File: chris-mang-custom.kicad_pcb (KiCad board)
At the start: 2 copper layers, 110 x 63.3 mm, 151 parts, among them J1 Barrel_Jack_Switch, J2 AudioJack_TRS, J3 AudioJack_TRS, J4 Conn_01x06, J5 Conn_01x06, Q1 Q_PMOS_GSD, Q2 2N7002, Q3 2N7002, Q4 2N7002, Q5 LS844, Q6 BC858C, Q7 LS844, Q8 BC858C, Q9 BC848C, SW1 SW_SPDT, SW2 SW_DPDT_x2, SW3 SW_DIP_SPDT_2pos, U1 DG412xY, U2 OPA2134, U3 TLV9352, U4 TLV9352

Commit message: first route of PCB
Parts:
- removed C34, C36: 8.2n, bca-footprints:C_Film_L7.2mm_W2.5mm_P5.00mm
- removed C35: 47p, Capacitor_SMD:C_0603_1608Metric_Pad1.08x0.95mm_HandSolder
- removed C37: 18n, bca-footprints:C_Film_L7.2mm_W2.5mm_P5.00mm
- removed C38: 39n, bca-footprints:C_Film_L7.2mm_W2.5mm_P5.00mm
- removed C39: 3.9n, bca-footprints:C_Film_L7.2mm_W2.5mm_P5.00mm
- removed C40: 5.6n, bca-footprints:C_Film_L7.2mm_W2.5mm_P5.00mm
- removed C41: 10u, Capacitor_SMD:C_0805_2012Metric_Pad1.18x1.45mm_HandSolder
- removed C42, C43: 100u, bca-footprints:CP_Radial_D6.3mm_P2.50mm
- removed C44, C45: 100n, Capacitor_SMD:C_0603_1608Metric_Pad1.08x0.95mm_HandSolder
- removed D12: 1N4148, Diode_SMD:D_SOD-323_HandSoldering
- removed Q7: LS844, Package_TO_SOT_SMD:SOT-23-6_Handsoldering
- removed Q8: BC858C, Package_TO_SOT_SMD:SOT-23_Handsoldering
- removed Q9: BC848C, Package_TO_SOT_SMD:SOT-23_Handsoldering
- removed R44: 15k, bca-footprints:R_L3.6mm_D1.6mm_P5.00mm_Horizontal
- removed R45, R58, R59: 10k, bca-footprints:R_L3.6mm_D1.6mm_P5.00mm_Horizontal
- removed R46: 22k, bca-footprints:R_L3.6mm_D1.6mm_P5.00mm_Horizontal
- removed R47: 1.5k, bca-footprints:R_L3.6mm_D1.6mm_P5.00mm_Horizontal
- removed R48, R55: 470k, bca-footprints:R_L3.6mm_D1.6mm_P5.00mm_Horizontal
- removed R49, R51, R53: 1M, Resistor_SMD:R_0805_2012Metric_Pad1.20x1.40mm_HandSolder
- removed R50, R56: 1k, bca-footprints:R_L3.6mm_D1.6mm_P5.00mm_Horizontal
- removed R52: 33k, Resistor_SMD:R_0805_2012Metric_Pad1.20x1.40mm_HandSolder
- removed R54: 6.8k, bca-footprints:R_L3.6mm_D1.6mm_P5.00mm_Horizontal
- removed R57: 100k, bca-footprints:R_L3.6mm_D1.6mm_P5.00mm_Horizontal
- removed R60, R61: 10k, Resistor_SMD:R_0805_2012Metric_Pad1.20x1.40mm_HandSolder
- removed SW3: SW_DIP_SPDT_2pos, bca-footprints:DIP-8_W7.62mm_Socket
- added RV9: 100kA, bca-footprints:R_POT, F.Cu at (45.0, -2.00)
- C14: footprint Capacitor_SMD:C_0603_1608Metric_Pad1.08x0.95mm_HandSolder -> Capacitor_SMD:C_0805_2012Metric_Pad1.18x1.45mm_HandSolder
- C16: value 0.15u -> 10n; footprint bca-footprints:C_Film_L7.2mm_W3.5mm_P5.00mm -> bca-footprints:C_Film_L7.2mm_W2.5mm_P5.00mm
- C17: value 47p -> 10n; footprint Capacitor_SMD:C_0603_1608Metric_Pad1.08x0.95mm_HandSolder -> bca-footprints:C_Film_L7.2mm_W2.5mm_P5.00mm
- C18: value 47p -> 100p; footprint Capacitor_SMD:C_0603_1608Metric_Pad1.08x0.95mm_HandSolder -> bca-footprints:C_Ceramic_L4.0mm_W2.5mm_P2.50mm
- C19: value 220p -> 0.1u; footprint bca-footprints:C_Ceramic_L4.0mm_W2.5mm_P2.50mm -> bca-footprints:C_Film_L7.2mm_W2.5mm_P5.00mm
- C20: value 0.1u -> 10n
- C21: value 47n -> 10n
- C22: value 3.9n -> 1u; footprint bca-footprints:C_Film_L7.2mm_W2.5mm_P5.00mm -> bca-footprints:C_Film_L7.2mm_W3.5mm_P5.00mm
- C23: footprint bca-footprints:C_Film_L7.2mm_W3.5mm_P5.00mm -> bca-footprints:CP_Radial_D4.0mm_P1.50mm
- C24, C25: value 100p -> 0.1u; footprint Capacitor_SMD:C_0603_1608Metric_Pad1.08x0.95mm_HandSolder -> bca-footprints:C_Film_L7.2mm_W2.5mm_P5.00mm
- C26: value 5.6n -> 22p; footprint bca-footprints:C_Film_L7.2mm_W2.5mm_P5.00mm -> bca-footprints:C_Ceramic_L4.0mm_W2.5mm_P2.50mm
- C27: value 5.6n -> 10u; footprint bca-footprints:C_Film_L7.2mm_W2.5mm_P5.00mm -> bca-footprints:CP_Radial_D4.0mm_P1.50mm
- C28: value 18n -> 10n
- C29: value 68n -> 10u; footprint bca-footprints:C_Film_L7.2mm_W2.5mm_P5.00mm -> bca-footprints:CP_Radial_D4.0mm_P1.50mm
- C30: value 33n -> 100u; footprint bca-footprints:C_Film_L7.2mm_W2.5mm_P5.00mm -> bca-footprints:CP_Radial_D6.3mm_P2.50mm
- C31: value 22p -> 100u; footprint Capacitor_SMD:C_0603_1608Metric_Pad1.08x0.95mm_HandSolder -> bca-footprints:CP_Radial_D6.3mm_P2.50mm
- C32: value 10u -> 100n
- C33: value 5.6n -> 100n; footprint bca-footprints:C_Film_L7.2mm_W2.5mm_P5.00mm -> Capacitor_SMD:C_0805_2012Metric_Pad1.18x1.45mm_HandSolder
- C6, C9: footprint Capacitor_SMD:C_0603_1608Metric_Pad1.08x0.95mm_HandSolder -> bca-footprints:C_Ceramic_L4.0mm_W2.5mm_P2.50mm
- D10: value 4v7 Zener -> 1N4148; footprint Diode_SMD:D_SOD-323_HandSoldering -> bca-footprints:Diode_DO-35_P5.00mm
- D11: value 1N4148 -> 1N5711; footprint Diode_SMD:D_SOD-323_HandSoldering -> bca-footprints:Diode_DO-35_P5.00mm
- D2, D3, D4, D5, D7, D8: footprint Diode_SMD:D_SOD-323_HandSoldering -> bca-footprints:Diode_DO-35_P5.00mm
- D6: value 1N5711 -> 1N4148; footprint Diode_SMD:D_SOD-323_HandSoldering -> bca-footprints:Diode_DO-35_P5.00mm
- D9: value 3v3 Zener -> 1N4148; footprint Diode_SMD:D_SOD-323_HandSoldering -> bca-footprints:Diode_DO-35_P5.00mm
- Q5: value LS844 -> BC848C; footprint Package_TO_SOT_SMD:SOT-23-6_Handsoldering -> Package_TO_SOT_SMD:SOT-23_Handsoldering
- Q6: value BC858C -> BC848C
- R19: value 10k -> 1M
- R20: value 1M -> 10k; footprint Resistor_SMD:R_0805_2012Metric_Pad1.20x1.40mm_HandSolder -> bca-footprints:R_L3.6mm_D1.6mm_P5.00mm_Horizontal
- R21: value 2.2k -> 27k; footprint Resistor_SMD:R_0603_1608Metric_Pad0.98x0.95mm_HandSolder -> bca-footprints:R_L3.6mm_D1.6mm_P5.00mm_Horizontal
- R22: value 4.7k -> 33k; footprint Resistor_SMD:R_0603_1608Metric_Pad0.98x0.95mm_HandSolder -> bca-footprints:R_L3.6mm_D1.6mm_P5.00mm_Horizontal
- R23: value 1.5k -> 1M
- R24: value 15k -> 10k
- R25, R31, R35: value 2.2k -> 100k; footprint Resistor_SMD:R_0603_1608Metric_Pad0.98x0.95mm_HandSolder -> bca-footprints:R_L3.6mm_D1.6mm_P5.00mm_Horizontal
- R26: value 56k -> 10k
- R27: value 330k -> 6.8k
- R28: value 1M -> 220k
- R29: value 15k -> 1k
- R30: value 470k -> 6.8k
- R32: value 4.7k -> 1M; footprint Resistor_SMD:R_0603_1608Metric_Pad0.98x0.95mm_HandSolder -> bca-footprints:R_L3.6mm_D1.6mm_P5.00mm_Horizontal
- R33: value 3.9k -> 10k
- R34: value 33k -> 100k
- R36: value 1k -> 100k
- R37: value 6.8k -> 10k
- R38: value 5.6k -> 1k
- R39: value 3.9k -> 1M
- R40: value 470k -> 10k
- R41: value 180k -> 22k
- R42: footprint bca-footprints:R_L3.6mm_D1.6mm_P5.00mm_Horizontal -> Resistor_SMD:R_0805_2012Metric_Pad1.20x1.40mm_HandSolder
- R43: value 22k -> 10k; footprint bca-footprints:R_L3.6mm_D1.6mm_P5.00mm_Horizontal -> Resistor_SMD:R_0805_2012Metric_Pad1.20x1.40mm_HandSolder
- RV5: value 250kA -> 100kB; footprint bca-footprints:R_POT_DUAL -> bca-footprints:R_POT
- RV6: value 100kA -> 25kB
- RV7: value 100k-CD -> 100kA; footprint bca-footprints:R_POT -> bca-footprints:R_POT_9mm
- RV8: value 100k-CD -> 100kA
- SW2: value SW_DPDT_x2 -> SW_DIP_SPDT_2pos; footprint bca-footprints:SW_Toggle_DPDT_SolderLug -> bca-footprints:DIP-8_W7.62mm_Socket; moved to F.Cu
- U3: value TLV9352 -> NJM4580
- moved Q5 60.6 mm to (50.6, -9.60)
- moved R43 56.3 mm to (17.2, -38.6), turned to -90 degrees
- moved R42 55.5 mm to (15.3, -38.6), turned to 90 degrees
- moved R34 53.4 mm to (50.6, -4.19), turned to 0 degrees
- moved R33 53.4 mm to (50.6, -6.47)
- moved Q6 51.9 mm to (50.6, 5.99)
- moved R39 51.7 mm to (50.6, 11.4), turned to 180 degrees
- moved R36 49.0 mm to (50.6, 0.36)
- moved C16 47.1 mm to (21.1, -28.5), turned to 180 degrees
- moved C15 46.7 mm to (21.1, -31.9), turned to 180 degrees
- moved R35 44.2 mm to (50.6, -1.92), turned to 0 degrees
- moved C28 43.7 mm to (40.9, 11.0), turned to 0 degrees
- moved R31 43.3 mm to (8.50, 10.3), turned to 180 degrees
- moved C27 42.0 mm to (38.7, 7.00), turned to 90 degrees
- moved RV6 41.0 mm to (15.0, -2.00)
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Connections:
- C15 pad 1: Net-(C15-Pad1) -> Earth
- C15 pad 2: Net-(Q5B-G1) -> Net-(C15-Pad2)
- C16 pad 1: Net-(C16-Pad1) -> Net-(C15-Pad2)
- C16 pad 2: Earth -> Net-(C16-Pad2)
- C17 pad 1: Net-(Q5A-G1) -> Net-(C17-Pad1)
- C17 pad 2: Net-(Q6-C) -> Net-(U3B-+)
- C18 pad 1: Net-(Q5B-D2) -> /bluesbreaker/sw2
- C18 pad 2: Net-(Q6-C) -> Net-(C18-Pad2)
- C19 pad 1: Net-(Q6-C) -> Net-(C19-Pad1)
- C20 pad 1: Net-(C20-Pad1) -> /bluesbreaker/4.5V
- C20 pad 2: Net-(D5-K) -> Net-(C20-Pad2)
- C21 pad 1: Net-(C20-Pad1) -> /bluesbreaker/4.5V
- C22 pad 1: Net-(D5-K) -> Net-(C22-Pad1)
- C22 pad 2: Net-(Q7B-G1) -> Net-(Q5-B)
- C23 pad 1: Net-(C23-Pad1) -> Net-(C22-Pad1)
- C23 pad 2: Earth -> Net-(Q5-B)
- C24 pad 1: Net-(D9-A) -> Net-(Q5-E)
- C24 pad 2: /blues-driver/sw_8 -> Net-(C24-Pad2)
- C25 pad 1: Net-(Q7B-D2) -> Net-(C25-Pad1)
- C25 pad 2: /blues-driver/sw_8 -> Net-(C25-Pad2)
- C26 pad 1: /blues-driver/sw_8 -> Net-(U4B--)
- C27 pad 1: Earth -> Net-(C26-Pad2)
- C28 pad 1: Earth -> /bluesbreaker-send
- C28 pad 2: Net-(C28-Pad2) -> Net-(Q6-B)
- C29 pad 1: /blues-driver/sw_6 -> Net-(Q6-E)
- C30 pad 1: /blues-driver/sw_3 -> /bluesbreaker/9V
- C30 pad 2: Net-(C29-Pad2) -> Earth
- C31 pad 1: Net-(U3B--) -> /bluesbreaker/4.5V
- C31 pad 2: Net-(C31-Pad2) -> Earth
- C32 pad 1: Net-(C31-Pad2) -> /bluesbreaker/9V
- C32 pad 2: /blues-driver/vol_out -> Earth
- C33 pad 1: Net-(U3A--) -> /bluesbreaker/9V
- C33 pad 2: Net-(C33-Pad2) -> Earth
- D10 pad 2: /blues-driver/sw_1 -> Net-(D10-A)
- D11 pad 1: Net-(D11-K) -> /bluesbreaker/sw3
- D11 pad 2: Net-(D11-A) -> Net-(D10-K)
- D6 pad 2: Earth -> Net-(D6-A)
- D7 pad 1: Net-(D7-K) -> /bluesbreaker/sw4
- D8 pad 1: Net-(D7-K) -> Net-(D6-A)
- D8 pad 2: Earth -> /bluesbreaker/sw4
- D9 pad 1: Net-(D10-K) -> Net-(D10-A)
- D9 pad 2: Net-(D9-A) -> /bluesbreaker/sw3
- FB3 pad 2: /blues-driver/9V -> /bluesbreaker/9V
- J5 pad 3: /bluesdriver-send -> /bluesbreaker-send
- J5 pad 4: /bluesdriver-return -> /bluesbreaker-return
- Q5 pad 1: Net-(Q5A-G1) -> Net-(Q5-B)
- Q5 pad 2: /blues-driver/9V -> Net-(Q5-E)
- Q5 pad 3: Net-(Q5A-S1) -> /bluesbreaker/9V
- Q6 pad 1: Net-(Q5B-D2) -> Net-(Q6-B)
- Q6 pad 2: /blues-driver/9V -> Net-(Q6-E)
- Q6 pad 3: Net-(Q6-C) -> /bluesbreaker/9V
- R19 pad 1: /bluesdriver-send -> Earth
- R19 pad 2: Net-(C15-Pad1) -> /bluesbreaker-send
- R20 pad 1: /blues-driver/4.5V -> /bluesbreaker-send
- R20 pad 2: Net-(Q5B-G1) -> Net-(C17-Pad1)
- R21 pad 1: Net-(Q5B-D2) -> Net-(C15-Pad2)
- R21 pad 2: /blues-driver/9V -> /bluesbreaker/sw2
- R22 pad 1: Earth -> Net-(C16-Pad2)
- R22 pad 2: Net-(Q5A-S1) -> /bluesbreaker/sw2
- R23 pad 1: Net-(C16-Pad1) -> /bluesbreaker/4.5V
- R23 pad 2: Net-(Q5A-G1) -> Net-(U3B-+)
- R24 pad 1: Net-(Q5A-G1) -> /bluesbreaker/sw7
- R24 pad 2: Net-(RV5A-4) -> Net-(R24-Pad2)
- R25 pad 1: Earth -> /bluesbreaker/sw2
- R25 pad 2: Net-(Q6-C) -> Net-(R24-Pad2)
- R26 pad 1: Net-(C20-Pad1) -> Net-(C19-Pad2)
- R26 pad 2: Net-(Q6-C) -> Net-(U3A--)
- R27 pad 1: Net-(D5-K) -> Net-(U3A--)
- R27 pad 2: Net-(C19-Pad2) -> Net-(D5-A)
- R28 pad 1: Net-(C21-Pad2) -> Net-(U3A--)
- R28 pad 2: Net-(D5-K) -> /bluesbreaker/sw5
- R29 pad 1: Earth -> /bluesbreaker/sw5
- R29 pad 2: Net-(C21-Pad2) -> Net-(D10-A)
- R30 pad 1: /blues-driver/4.5V -> Net-(R30-Pad1)
- R30 pad 2: Net-(Q7B-G1) -> Net-(R30-Pad2)
- R31 pad 1: Net-(Q7B-D2) -> Net-(C21-Pad2)
- R31 pad 2: /blues-driver/9V -> Net-(R30-Pad2)
- R32 pad 1: Earth -> /bluesbreaker/4.5V
- R32 pad 2: Net-(Q7A-S1) -> Net-(Q5-B)
- R33 pad 1: Net-(C23-Pad1) -> Earth
- R33 pad 2: Net-(D9-A) -> Net-(Q5-E)
- R34 pad 1: Net-(D9-A) -> Net-(C24-Pad2)
- R34 pad 2: Net-(R34-Pad2) -> Net-(U4B--)
- R35 pad 1: Earth -> Net-(C25-Pad2)
- R35 pad 2: /blues-driver/sw_8 -> Net-(U4B--)
- R36 pad 1: Net-(C26-Pad2) -> Net-(U4B--)
- R36 pad 2: Net-(C27-Pad2) -> Net-(C26-Pad2)
- R37 pad 1: /blues-driver/sw_8 -> Earth
- R38 pad 2: /blues-driver/sw_3 -> /bluesbreaker-return
- R39 pad 1: Net-(C28-Pad2) -> /bluesbreaker/4.5V
- R39 pad 2: /blues-driver/sw_3 -> Net-(Q6-B)
- R40 pad 1: Net-(R40-Pad1) -> Earth
- R40 pad 2: Net-(U3B--) -> Net-(Q6-E)
- R41 pad 1: Net-(U3B--) -> Net-(C29-Pad2)
- R41 pad 2: Net-(C31-Pad2) -> Net-(U4A--)
- R42 pad 1: /blues-driver/vol_out -> /bluesbreaker/4.5V
- R42 pad 2: Net-(R42-Pad2) -> /bluesbreaker/9V
- R43 pad 1: /blues-driver/vol_out -> Earth
- R43 pad 2: Net-(C34-Pad2) -> /bluesbreaker/4.5V
- RV5 pad 1: Net-(RV5A-4) -> Net-(R24-Pad2)
- RV5 pad 2: Net-(Q6-C) -> Net-(C18-Pad2)
- RV5 pad 3: Net-(Q6-C) -> Net-(C19-Pad1)
- RV6 pad 1: /blues-driver/4.5V -> Net-(C20-Pad2)
- RV6 pad 2: Net-(R40-Pad1) -> Net-(R30-Pad1)
- RV6 pad 3: Net-(C29-Pad2) -> Net-(D10-A)
- RV7 pad 1: Net-(R45-Pad1) -> Net-(C21-Pad2)
- RV7 pad 2: Net-(C33-Pad2) -> Net-(R30-Pad2)
- RV7 pad 3: Net-(R42-Pad2) -> Net-(R30-Pad2)
- RV8 pad 1: Net-(C34-Pad1) -> /bluesbreaker/4.5V
- RV8 pad 2: Net-(R44-Pad1) -> Net-(C22-Pad1)
- RV8 pad 3: Net-(C34-Pad2) -> Net-(R30-Pad2)
- SW2 pad 1: Net-(SW2A-A) -> unconnected-(SW2A-C-Pad1)
- SW2 pad 2: Net-(D11-A) -> /bluesbreaker/sw2
- SW2 pad 3: Net-(SW2A-C) -> /bluesbreaker/sw3
- SW2 pad 4: Net-(SW2B-A) -> /bluesbreaker/sw4
- SW2 pad 5: Net-(D11-K) -> /bluesbreaker/sw5
- SW2 pad 6: unconnected-(SW2B-C-Pad6) -> /bluesbreaker/4.5V
- U3 pad 1: Net-(C35-Pad2) -> /bluesbreaker/sw5
- U3 pad 3: /blues-driver/4.5V -> /bluesbreaker/4.5V
- U3 pad 5: /blues-driver/4.5V -> Net-(U3B-+)
- U3 pad 6: Net-(U3B--) -> /bluesbreaker/sw2
- U3 pad 7: Net-(C31-Pad2) -> Net-(C18-Pad2)
- U3 pad 8: /blues-driver/9V -> /bluesbreaker/9V
- U4 pad 1: Net-(C39-Pad2) -> Net-(C25-Pad1)
- U4 pad 2: Net-(D11-K) -> Net-(U4A--)
- U4 pad 3: Net-(D11-A) -> /bluesbreaker/4.5V
- U4 pad 5: Net-(U4B-+) -> /bluesbreaker/4.5V
- U4 pad 7: Net-(U4B--) -> Net-(C26-Pad2)
- U4 pad 8: /blues-driver/9V -> /bluesbreaker/9V

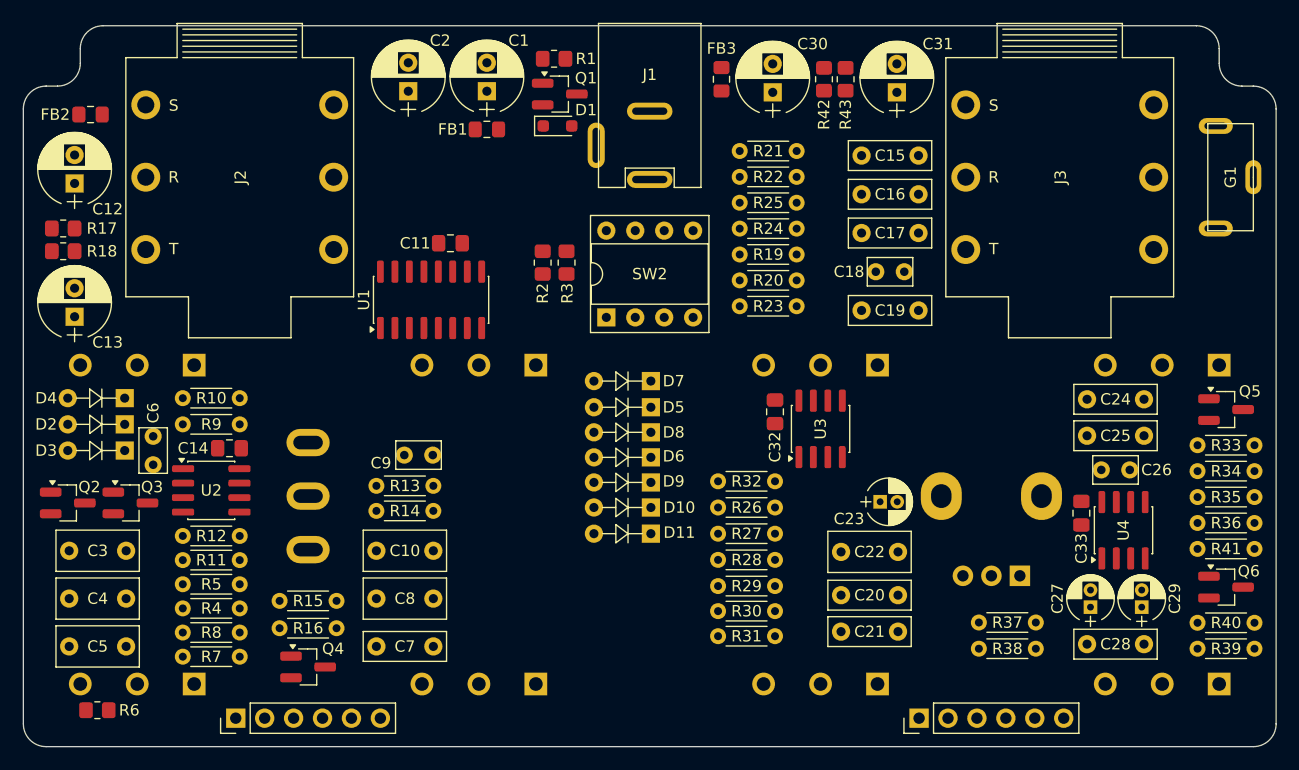
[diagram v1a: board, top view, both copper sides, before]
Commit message: finalized schematic
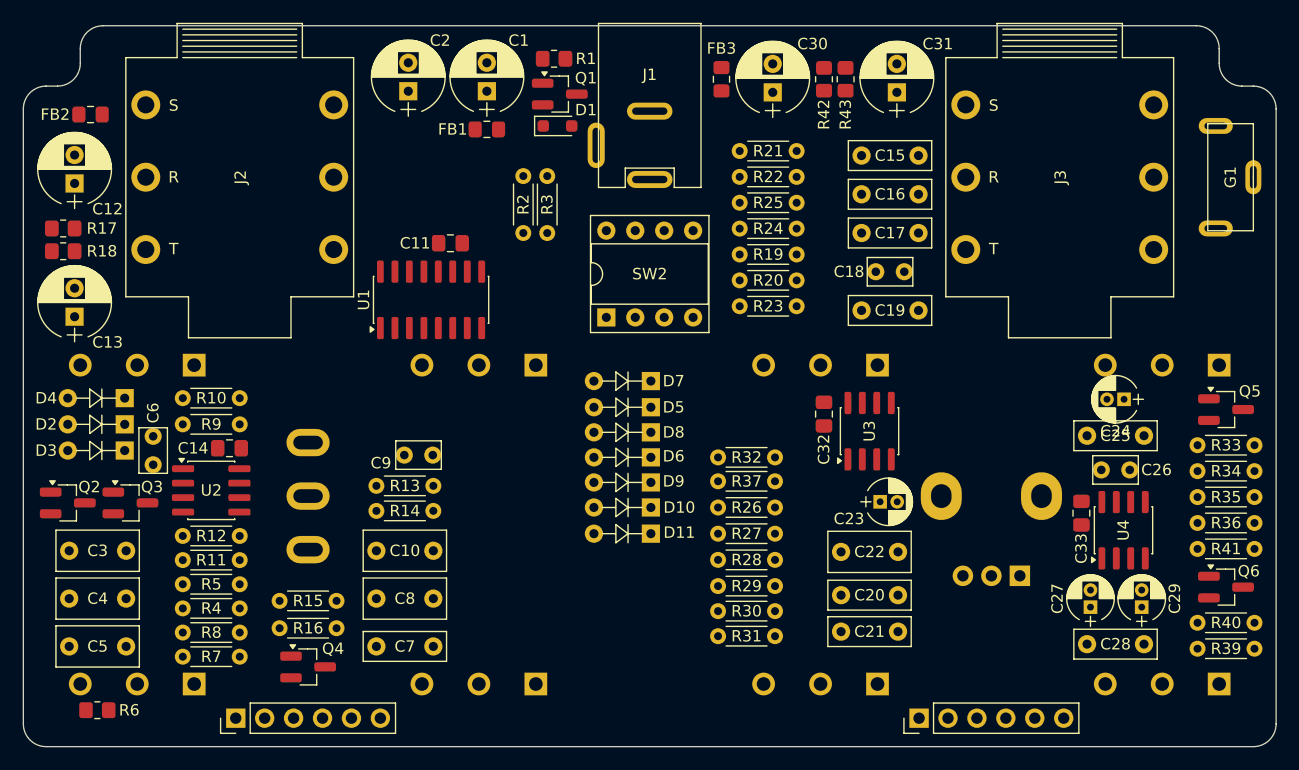
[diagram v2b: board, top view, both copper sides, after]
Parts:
- removed R38: 1k, bca-footprints:R_L3.6mm_D1.6mm_P5.00mm_Horizontal
- C24: value 0.1u -> 10u; footprint bca-footprints:C_Film_L7.2mm_W2.5mm_P5.00mm -> bca-footprints:CP_Radial_D4.0mm_P1.50mm
- C25: value 0.1u -> 47n
- C26: value 22p -> 47p
- R2, R3: footprint Resistor_SMD:R_0805_2012Metric_Pad1.20x1.40mm_HandSolder -> bca-footprints:R_L3.6mm_D1.6mm_P5.00mm_Horizontal
- R36: value 100k -> 180k
- R37: value 10k -> 100k
- R41: value 22k -> 10k
- moved R37 26.0 mm to (8.50, -3.30), turned to 0 degrees
- moved R3 5.38 mm to (-9.00, -27.6)
- moved R2 5.38 mm to (-11.1, -27.6)
- moved C32 4.30 mm to (15.3, -9.20)
- moved U3 4.30 mm to (19.3, -7.70)
- moved R32 2.10 mm to (8.50, -5.40)
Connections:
- R30 pad 2: Net-(R30-Pad2) -> Net-(C22-Pad1)
- R31 pad 2: Net-(R30-Pad2) -> Net-(C22-Pad1)
- R37 pad 1: Earth -> /bluesbreaker/4.5V
- R37 pad 2: Net-(C27-Pad2) -> Net-(C22-Pad1)
- RV7 pad 2: Net-(R30-Pad2) -> Net-(C22-Pad1)
- RV7 pad 3: Net-(R30-Pad2) -> Net-(C22-Pad1)
- RV8 pad 1: /bluesbreaker/4.5V -> Earth
- RV8 pad 2: Net-(C22-Pad1) -> /bluesbreaker-return
- RV8 pad 3: Net-(R30-Pad2) -> Net-(C27-Pad2)

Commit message: first draft PCB
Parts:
- added C34: 100p, bca-footprints:C_Ceramic_L4.0mm_W2.5mm_P2.50mm, F.Cu at (50.0, -1.30)
- R24: value 10k -> 33k
- R25: value 100k -> 150k
- moved C27 27.7 mm to (49.7, -18.4), turned to 0 degrees
- moved R33 24.6 mm to (26.4, -10.6), turned to 0 degrees
- moved Q5 23.1 mm to (27.7, -6.90)
- moved R31 21.6 mm to (30.0, 8.20)
- moved R39 20.6 mm to (30.0, 11.2), turned to 0 degrees
- moved R32 19.5 mm to (26.5, -12.8)
- moved Q4 18.6 mm to (-11.7, 9.80)
- moved R15 18.6 mm to (-11.7, 4.00), turned to 180 degrees
- moved R16 18.6 mm to (-11.7, 6.40), turned to 180 degrees
- moved R10 9.39 mm to (-30.0, -14.6)
- moved R4 9.25 mm to (-30.0, 11.5), turned to 180 degrees
- moved R9 8.95 mm to (-30.0, -11.1)
- moved R26 8.90 mm to (8.50, -9.90)
- moved R5 8.85 mm to (-30.0, 8.20)
- moved R27 8.24 mm to (8.50, -6.94)
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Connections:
- C18 pad 1: /bluesbreaker/sw2 -> /bluesbreaker/sw7
- R21 pad 2: /bluesbreaker/sw2 -> /bluesbreaker/sw7
- R22 pad 2: /bluesbreaker/sw2 -> /bluesbreaker/sw7
- R24 pad 1: /bluesbreaker/sw7 -> /bluesbreaker/sw2
- R25 pad 1: /bluesbreaker/sw2 -> /bluesbreaker/sw7
- U1 pad 1: /Zendrive/Q1D -> /Zendrive/Q1G
- U1 pad 10: Net-(D2-A) -> Net-(C4-Pad1)
- U1 pad 11: Net-(D4-A) -> Earth
- U1 pad 14: (no net) -> Net-(D4-A)
- U1 pad 15: (no net) -> Net-(D2-A)
- U1 pad 16: (no net) -> /Zendrive/Q1D
- U1 pad 2: Net-(C4-Pad1) -> Net-(R9-Pad2)
- U1 pad 3: Earth -> Net-(D4-A)
- U1 pad 6: Net-(R9-Pad2) -> (no net)
- U1 pad 7: Net-(D4-A) -> (no net)
- U1 pad 8: /Zendrive/Q1G -> (no net)
- U3 pad 6: /bluesbreaker/sw2 -> /bluesbreaker/sw7
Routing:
- net /bluesbreaker/4.5V: track 0.00 -> 170.2 mm, vias 0 -> 3
- net /bluesbreaker/9V: track 0.00 -> 122.8 mm, vias 0 -> 4
- net /Zendrive/9V: track 0.00 -> 110.1 mm, vias 0 -> 2
- net /bluesbreaker-send: track 0.00 -> 104.3 mm
- net +9V: track 0.00 -> 101.2 mm
- net /V+1: track 0.00 -> 90.3 mm
- net Net-(C4-Pad1): track 0.00 -> 89.9 mm, vias 0 -> 1
- net /output_jack: track 0.00 -> 86.3 mm
- net Net-(D4-A): track 0.00 -> 83.9 mm, vias 0 -> 2
- net /input_jack: track 0.00 -> 69.9 mm
- net /Zendrive/Q1G: track 0.00 -> 67.6 mm, vias 0 -> 1
- net /bluesbreaker-return: track 0.00 -> 64.2 mm
- net /bluesbreaker/sw7: track 0.00 -> 63.1 mm
- net Net-(D3-A): track 0.00 -> 62.1 mm
- net /V+0: track 0.00 -> 61.6 mm
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- added copper zone on In1.Cu, net Earth
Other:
- copper layers 2 -> 4

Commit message: generated gerbers
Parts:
- C22: footprint bca-footprints:C_Film_L7.2mm_W3.5mm_P5.00mm -> bca-footprints:C_Film_L7.2mm_W5.00mm_P5.00mm
- R24: value 33k -> 39k
- moved C20 1.30 mm to (18.6, 8.10)
- moved C28 1.00 mm to (40.1, 11.1)
- moved C29 0.81 mm to (40.1, 6.60)
- moved C22 0.80 mm to (18.6, 3.80)
- moved C21 0.50 mm to (18.6, 11.1)
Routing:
- net Net-(C22-Pad1): track 34.9 -> 37.4 mm
- net Net-(Q6-B): track 33.8 -> 32.2 mm
- net /bluesbreaker/4.5V: track 170.2 -> 168.6 mm
- net Net-(C20-Pad2): track 8.90 -> 7.60 mm
- net Net-(C4-Pad1): track 89.9 -> 88.6 mm
- net Net-(Q5-B): track 20.6 -> 21.4 mm
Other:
- board text added: "Bennett Custom Audio Custom Dual OD v1.0.0; Mar 2026"
- board text added: "Designed & Assembled in St. John's, NL"
- board text added: "HI GAIN ->"
- board text added: "OD -> DIST"

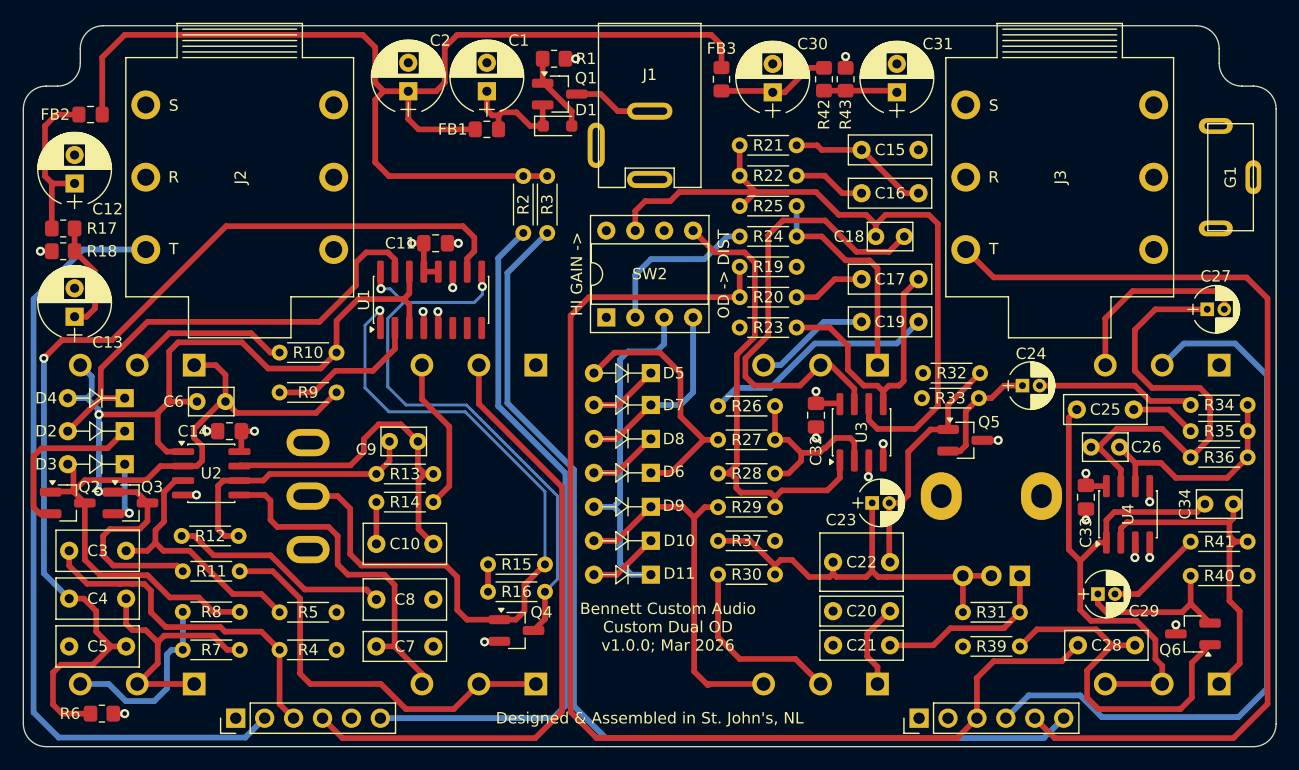
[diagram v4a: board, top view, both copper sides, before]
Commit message: re-generated gerbers, finalized BOM
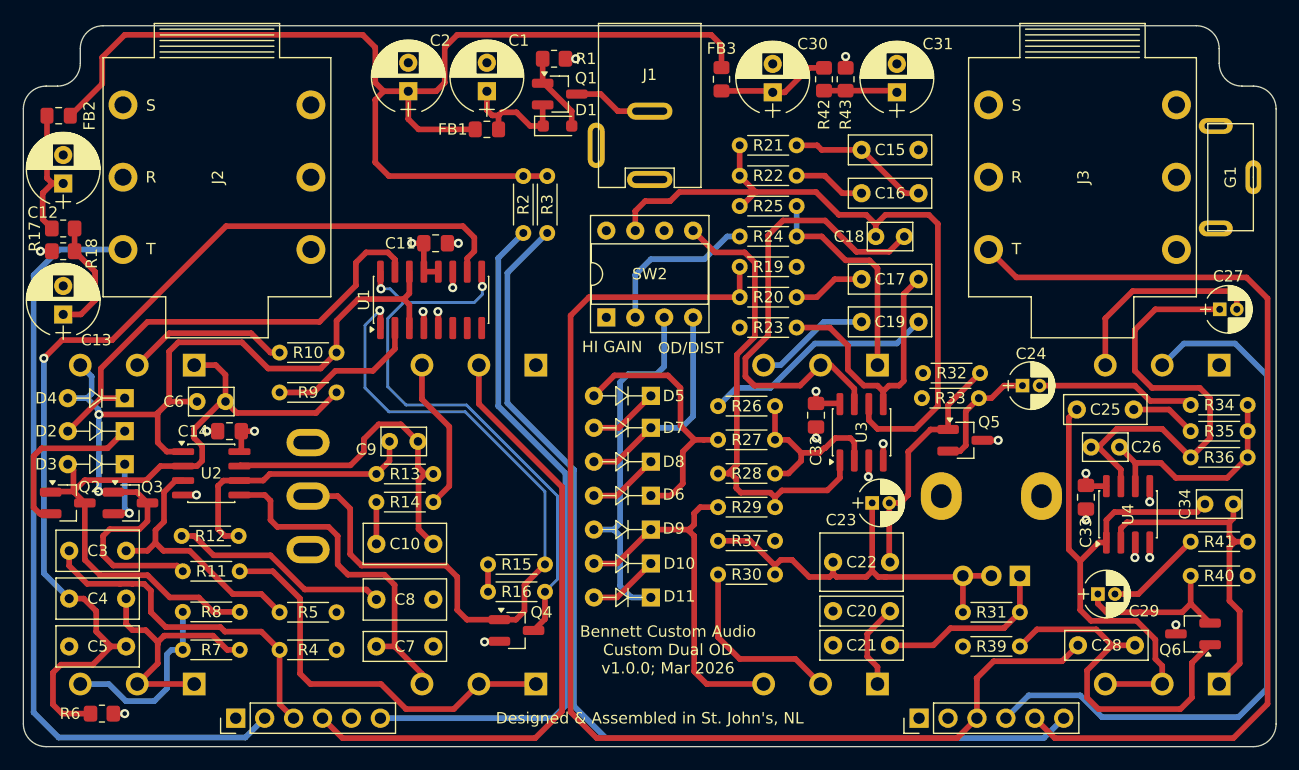
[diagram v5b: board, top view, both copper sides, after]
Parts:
- moved FB2 2.80 mm to (-51.9, -35.4)
- moved D10 2.00 mm to (-2.40, 3.92)
- moved D11 2.00 mm to (-2.40, 6.90)
- moved D5 2.00 mm to (-2.40, -10.8)
- moved D6 2.00 mm to (-2.40, -2.04)
- moved D7 2.00 mm to (-2.40, -8.00)
- moved D8 2.00 mm to (-2.40, -5.02)
- moved D9 2.00 mm to (-2.40, 0.94)
- moved J2 2.00 mm to (-38.0, -30.0)
- moved J3 2.00 mm to (38.0, -30.0)
- moved C27 1.10 mm to (50.8, -18.4)
- moved C13 1.02 mm to (-51.5, -19.2)
- moved C12 1.00 mm to (-51.5, -30.7)
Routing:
- net /Zendrive/9V: track 110.1 -> 106.5 mm
- net /bluesbreaker/9V: track 122.8 -> 125.4 mm
- net /bluesbreaker/sw4: track 17.0 -> 19.0 mm
- net /output_jack: track 86.3 -> 84.3 mm
- net /bluesbreaker/sw3: track 30.0 -> 32.0 mm
- net +9V: track 101.2 -> 102.4 mm
- net Net-(C27-Pad2): track 16.7 -> 17.9 mm
- net Net-(C26-Pad2): track 38.9 -> 40.0 mm
- net /input_jack: track 69.9 -> 69.1 mm
- net /Zendrive/4.5V: track 54.6 -> 55.3 mm
- net Net-(D5-A): track 22.9 -> 23.4 mm
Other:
- board text added: "HI GAIN"
- board text added: "OD/DIST"
- board text removed: "HI GAIN ->"
- board text removed: "OD -> DIST"
